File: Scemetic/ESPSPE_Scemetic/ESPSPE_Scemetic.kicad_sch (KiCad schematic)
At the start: 38 parts, among them SW1 RESET, U1 ADIN1110, Y1 25MHz

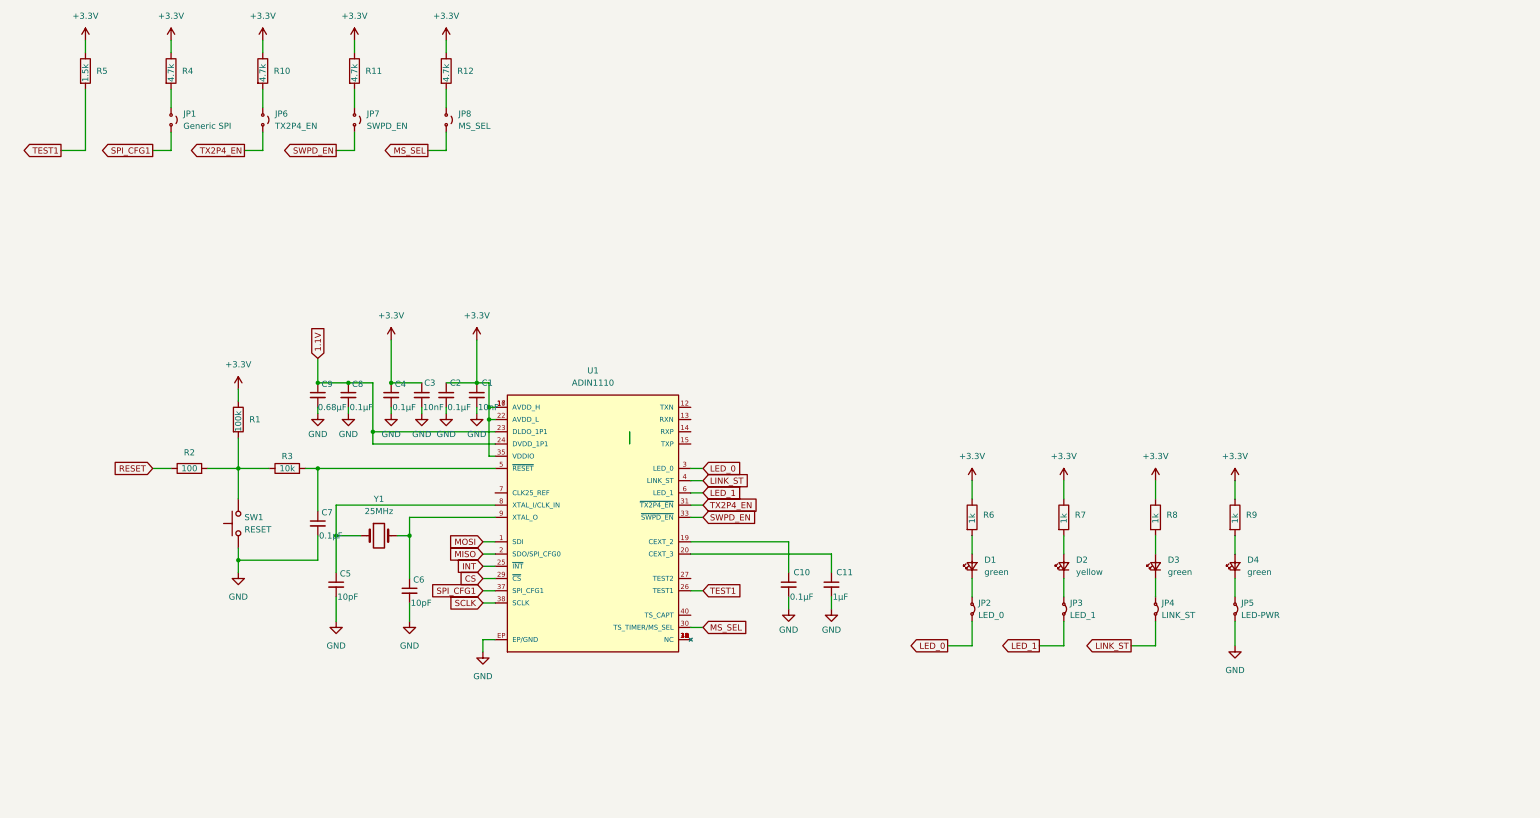
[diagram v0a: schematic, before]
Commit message: added ESP Pinout; Update of Scemetic -> should be ready to search for components
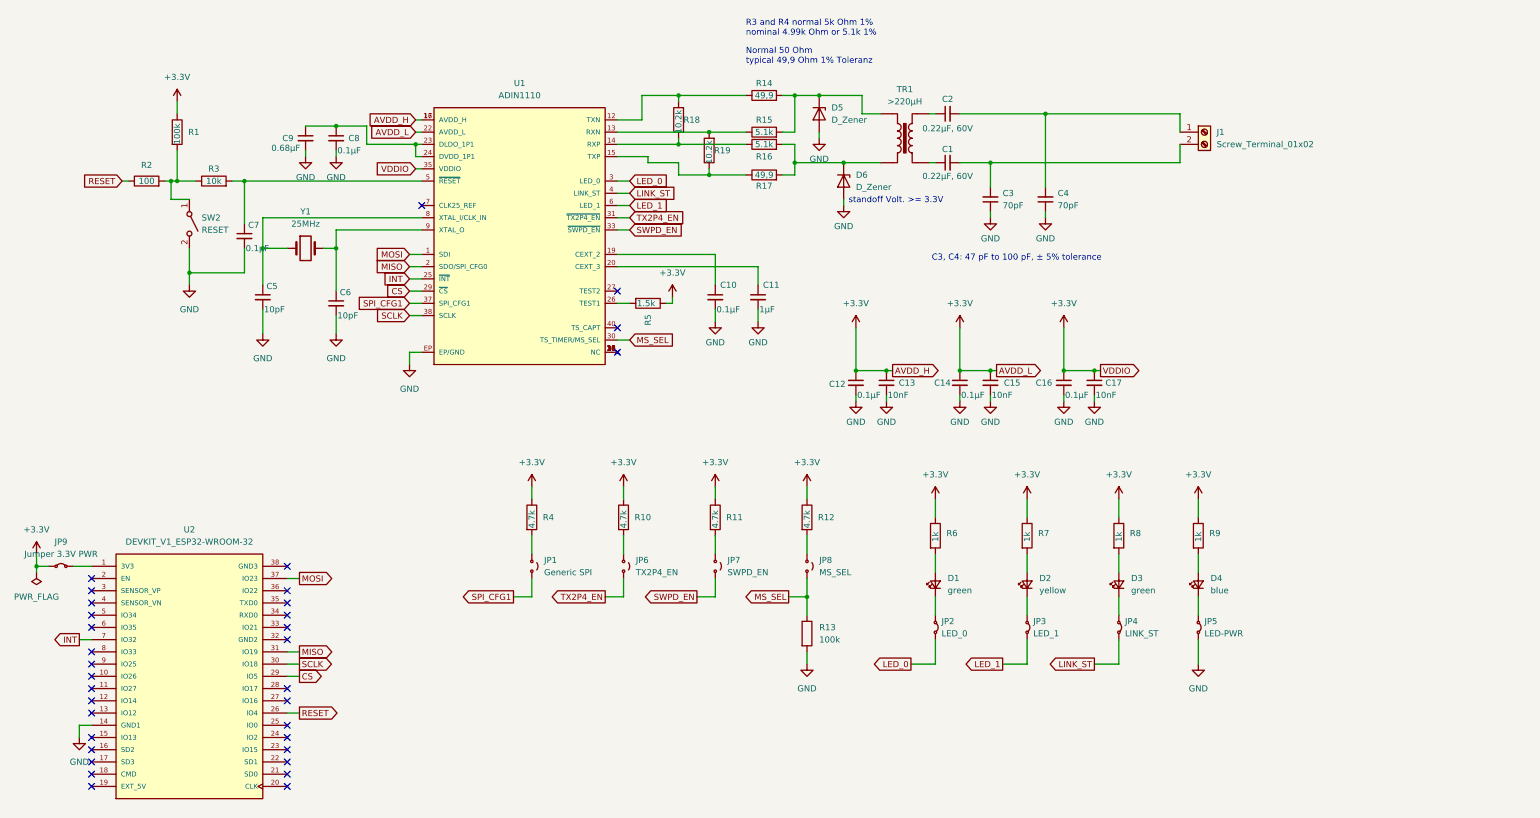
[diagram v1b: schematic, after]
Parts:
- removed SW1: RESET, symbol Switch:SW_Push
- added C12, C14, C16: 0.1µF, symbol Device:C_Small
- added C13, C15, C17: 10nF, symbol Device:C_Small
- added D5, D6: D_Zener, symbol Device:D_Zener
- added J1: Screw_Terminal_01x02, symbol Connector:Screw_Terminal_01x02
- added JP9: Jumper 3.3V PWR, symbol Jumper:Jumper_2_Small_Bridged
- added R13: 100k, symbol Device:R
- added R14, R17: 49,9, symbol Device:R
- added R15, R16: 5.1k, symbol Device:R
- added R18, R19: 10.2k, symbol Device:R
- added SW2: RESET, symbol Switch:SW_SPST
- added TR1: >220µH, symbol Transformer:TRANSF1
- added U2: DEVKIT_V1_ESP32-WROOM-32, DEVKIT_V1_ESP32-WROOM-32:MODULE_DEVKIT_V1_ESP32-WROOM-32, symbol DEVKIT_V1_ESP32-WROOM-32:DEVKIT_V1_ESP32-WROOM-32
- C1: value 10nF -> 0.22µF, 60V
- C2: value 0.1µF -> 0.22µF, 60V
- C3: value 10nF -> 70pF
- C4: value 0.1µF -> 70pF
- D4: value green -> blue
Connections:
- net +3.3V: now also C12.1, C13.1, C14.1, C15.1, C16.1, C17.1, JP9.1 (A); no longer C1.1, C2.1, C3.1, C4.1
- net CS: now also U2.29 (IO5)
- net GND: now also C3.1, C4.1, C12.2, C13.2, C14.2, C15.2, C16.2, C17.2, D5.2 (A), D6.2 (A), R13.2, SW2.2 (B), U2.14 (GND1); no longer C1.2, C2.2, C3.2, C4.2
- net INT: now also U2.7 (IO32)
- net MISO: now also U2.31 (IO19)
- net MOSI: now also U2.37 (IO23)
- net MS_SEL: now also R13.1
- net RESET: now also U2.26 (IO4)
- net SCLK: now also U2.30 (IO18)
- net at R1.2, R2.2, R3.1: now also SW2.1 (A)
- net at U1.12 (TXN): now also R14.1, R18.2
- net at U1.13 (RXN): now also R15.1, R19.2
- net at U1.14 (RXP): now also R16.1, R18.1
- net at U1.15 (TXP): now also R17.1, R19.1
- net 1.1V: no longer names the net of C8.1, C9.1, U1.23 (DLDO_1P1), U1.24 (DVDD_1P1)
- net TEST1: no longer names the net of R5.2, U1.26 (TEST1)
- new net: D5.1 (K), R14.2, R15.2, TR1.1
- new net: C2.2, C4.2, J1.1 (Pin_1)
- new net: JP9.2 (B), U2.1 (3V3)
- new net: C1.1, TR1.3
- new net: C1.2, C3.2, J1.2 (Pin_2)
- new net: C2.1, TR1.4
- new net: D6.1 (K), R16.2, R17.2, TR1.2
- no-connect marks 0 -> 34
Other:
- note added: "C3, C4: 47 pF to 100 pF, ± 5% tolerance"
- note added: "Normal 50 Ohm typical 49,9 Ohm 1% Toleranz"
- note added: "R3 and R4 normal 5k Ohm 1% nominal 4.99k Ohm or 5.1k 1%"
- note added: "standoff Volt. >= 3.3V"
- moved on the sheet: C10, C11, C5, C6, C7, C8, C9, D1, D2, D3, D4, JP1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

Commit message: Schaltplan vollständig
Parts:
- renumbered C7 to C1, C2 to C10, C1 to C11, C14 to C12, C3 to C13, C15 to C14, C4 to C15, C5 to C2, C9 to C3, C8 to C4, C6 to C5, C10 to C6, C11 to C7, C12 to C8, C13 to C9, D5 to D1, D6 to D2, D1 to D3, D2 to D4, D3 to D5, D4 to D6, JP9 to JP1, JP1 to JP2, JP6 to JP3, JP7 to JP4, JP8 to JP5, JP2 to JP6, JP3 to JP7, JP4 to JP8, JP5 to JP9, R2 to R1, R14 to R10, R15 to R11, R16 to R12, R17 to R13, R12 to R14, R13 to R15, R6 to R16, R7 to R17, R8 to R18, R9 to R19, R1 to R2, R10 to R5, R5 to R6, R18 to R7, R19 to R8, R11 to R9, SW2 to SW1, U2 to U1, U1 to U2

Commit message: Schaltplan Footprintzuweisung angefangen
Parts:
- removed TR1: >220µH, symbol Transformer:TRANSF1
- added T1: 749070010, Transformer_SMD_Wurth:T_Wurth_WE-SPE_749070010, symbol Transformer_Wurth_WE-SPE:749070010
- added Y2: CFPX-180_830105863709, Crystal_SMD_Wurth:Y_Wurth_WE-XTAL-CFPX-180, symbol Crystal_Wurth_WE-XTAL:CFPX-180_830105863709
- C1, C10, C11, C12, C13, C14, C15, C16, C17, C2, C3, C4, C5, C6, C7, C8, C9: footprint (none) -> Capacitor_SMD:C_0805_2012Metric_Pad1.18x1.45mm_HandSolder
- D3, D5: footprint (none) -> LED_THT:LED_D3.0mm
- D4: value yellow -> green; footprint (none) -> LED_THT:LED_D3.0mm
- D6: value blue -> green; footprint (none) -> LED_THT:LED_D3.0mm
- J1: footprint (none) -> TerminalBlock_Phoenix:TerminalBlock_Phoenix_MPT-0,5-2-2.54_1x02_P2.54mm_Horizontal
- JP1, JP2, JP3, JP4, JP5, JP6, JP7, JP8, JP9: footprint (none) -> Connector_PinHeader_2.54mm:PinHeader_1x02_P2.54mm_Vertical
- R1, R10, R11, R12, R13, R14, R15, R16, R17, R18, R19, R2, R3, R4, R5, R6, R7, R8, R9: footprint (none) -> Resistor_SMD:R_0805_2012Metric_Pad1.20x1.40mm_HandSolder
- SW1: footprint (none) -> Button_Switch_THT:SW_PUSH_6mm
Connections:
- net at D1.1 (K), R10.2, R11.2: now also T1.1
- net at C11.1: now also T1.3
- net at C10.1: now also T1.2
- net at D2.1 (K), R12.2, R13.2: now also T1.4
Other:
- note added: "Benötigen wir hier eine spezielle Bauform / Marke?"
- note added: "Kondensatoren so nah wie möglich an IC platzieren"
- moved on the sheet: C10, C11, C13, C15, J1

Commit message: Jumper für PWR LED entfernt. Footprint für Traffo und Quartz zugewiesen. Z_Diode 0805 zugewiesen. Platine angefangen zu zeichen -> Bauteile angeordnet
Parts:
- removed JP9: LED-PWR, Connector_PinHeader_2.54mm:PinHeader_1x02_P2.54mm_Vertical, symbol Jumper:Jumper_2_Small_Bridged
- removed Y1: 25MHz, symbol Device:Crystal
- C2, C5: value 10pF -> 15pF
- D1, D2: footprint (none) -> Diode_SMD:D_0805_2012Metric_Pad1.15x1.40mm_HandSolder
- Y2: footprint Crystal_SMD_Wurth:Y_Wurth_WE-XTAL-CFPX-180 -> Crystal_SMD_Wurth:Y_Wurth_WE-XTAL_Quartz-CFPX-180
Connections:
- net GND: now also D6.1 (K), Y2.2 (GND), Y2.4 (GND1)
- net at Y2.1: now also C2.1, U2.8 (XTAL_I/CLK_IN)
- net at Y2.3: now also C5.1, U2.9 (XTAL_O)
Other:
- note added: "25MHz"
- note added: "C13, C15: 47 pF to 100 pF, ± 5% tolerance"
- note removed: "C3, C4: 47 pF to 100 pF, ± 5% tolerance"
- moved on the sheet: C12, C14, C16, C17, C8, C9, D1, D2, Y2

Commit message: Jumper der LEDs entfernt
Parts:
- removed JP6: LED_0, Connector_PinHeader_2.54mm:PinHeader_1x02_P2.54mm_Vertical, symbol Jumper:Jumper_2_Small_Bridged
- removed JP7: LED_1, Connector_PinHeader_2.54mm:PinHeader_1x02_P2.54mm_Vertical, symbol Jumper:Jumper_2_Small_Bridged
- removed JP8: LINK_ST, Connector_PinHeader_2.54mm:PinHeader_1x02_P2.54mm_Vertical, symbol Jumper:Jumper_2_Small_Bridged
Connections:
- net LED_0: now also D3.1 (K)
- net LED_1: now also D4.1 (K)
- net LINK_ST: now also D5.1 (K)
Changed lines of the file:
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@@
 	(wire
 		(pts
-			(xy 210.82 152.4) (xy 210.82 157.48)
+			(xy 210.82 143.51) (xy 210.82 157.48)
 		)
 		(stroke
@@
 	(wire
 		(pts
-			(xy 210.82 143.51) (xy 210.82 147.32)
-		)
-		(stroke
-			(width 0)
-			(type default)
-		)
-	)
-	(wire
-		(pts
 			(xy 33.02 152.4) (xy 35.56 152.4)
 		)
@@
 	(wire
 		(pts
+			(xy 248.92 143.51) (xy 248.92 157.48)
+		)
+		(stroke
+			(width 0)
+			(type default)
+		)
+	)
+	(wire
+		(pts
 			(xy 229.87 134.62) (xy 229.87 138.43)
 		)
@@
 	(wire
 		(pts
-			(xy 229.87 143.51) (xy 229.87 147.32)
-		)
-		(stroke
-			(width 0)
-			(type default)
-		)
-	)
-	(wire
-		(pts
-			(xy 248.92 152.4) (xy 248.92 157.48)
+			(xy 229.87 143.51) (xy 229.87 157.48)
 		)
 		(stroke
@@
 	(wire
 		(pts
-			(xy 229.87 152.4) (xy 229.87 157.48)
-		)
-		(stroke
-			(width 0)
-			(type default)
-		)
-	)
-	(wire
-		(pts
 			(xy 181.61 55.88) (xy 181.61 53.34)
 		)
@@
 	(wire
 		(pts
-			(xy 248.92 143.51) (xy 248.92 147.32)
-		)
-		(stroke
-			(width 0)
-			(type default)
-		)
-	)
-	(wire
-		(pts
 			(xy 151.13 52.07) (xy 144.78 52.07)
 		)
@@
 	)
 	(symbol
-		(lib_id "Jumper:Jumper_2_Small_Bridged")
-		(at 248.92 149.86 270)
-		(unit 1)
-		(exclude_from_sim no)
-		(in_bom yes)
-		(on_board yes)
-		(dnp no)
-		(fields_autoplaced yes)
-		(property "Reference" "JP8"
-			(at 250.19 148.5899 90)
-			(effects
-				(font
-					(size 1.27 1.27)
-				)
-				(justify left)
-			)
-		)
-		(property "Value" "LINK_ST"
-			(at 250.19 151.1299 90)
-			(effects
-				(font
-					(size 1.27 1.27)
-				)
-				(justify left)
-			)
-		)
-		(property "Footprint" "Connector_PinHeader_2.54mm:PinHeader_1x02_P2.54mm_Vertical"
-			(at 248.92 149.86 0)
-			(effects
-				(font
-					(size 1.27 1.27)
-				)
-				(hide yes)
-			)
-		)
-		(property "Datasheet" "~"
-			(at 248.92 149.86 0)
-			(effects
-				(font
-					(size 1.27 1.27)
-				)
-				(hide yes)
-			)
-		)
-		(property "Description" "Jumper, 2-pole, small symbol, bridged"
-			(at 248.92 149.86 0)
-			(effects
-				(font
-					(size 1.27 1.27)
-				)
-				(hide yes)
-			)
-		)
-		(pin "1"
-		)
-		(pin "2"
-		)
-		(instances
-			(project "ESPSPE_Scemetic"
-				(path "/a7aa0af1-99b4-4491-b08a-049990c2f2ac"
-					(reference "JP8")
-					(unit 1)
-				)
-			)
-		)
-	)
-	(symbol
 		(lib_id "Jumper:Jumper_2_Small_Open")
 		(at 127 137.16 270)
@@
 	)
 	(symbol
-		(lib_id "Jumper:Jumper_2_Small_Bridged")
-		(at 229.87 149.86 270)
-		(unit 1)
-		(exclude_from_sim no)
-		(in_bom yes)
-		(on_board yes)
-		(dnp no)
-		(fields_autoplaced yes)
-		(property "Reference" "JP7"
-			(at 231.14 148.5899 90)
-			(effects
-				(font
-					(size 1.27 1.27)
-				)
-				(justify left)
-			)
-		)
-		(property "Value" "LED_1"
-			(at 231.14 151.1299 90)
-			(effects
-				(font
-					(size 1.27 1.27)
-				)
-				(justify left)
-			)
-		)
-		(property "Footprint" "Connector_PinHeader_2.54mm:PinHeader_1x02_P2.54mm_Vertical"
-			(at 229.87 149.86 0)
-			(effects
-				(font
-					(size 1.27 1.27)
-				)
-				(hide yes)
-			)
-		)
-		(property "Datasheet" "~"
-			(at 229.87 149.86 0)
-			(effects
-				(font
-					(size 1.27 1.27)
-				)
-				(hide yes)
-			)
-		)
-		(property "Description" "Jumper, 2-pole, small symbol, bridged"
-			(at 229.87 149.86 0)
-			(effects
-				(font
-					(size 1.27 1.27)
-				)
-				(hide yes)
-			)
-		)
-		(pin "1"
-		)
-		(pin "2"
-		)
-		(instances
-			(project "ESPSPE_Scemetic"
-				(path "/a7aa0af1-99b4-4491-b08a-049990c2f2ac"
-					(reference "JP7")
-					(unit 1)
-				)
-			)
-		)
-	)
-	(symbol
 		(lib_id "power:GND")
 		(at 222.25 104.14 0)
@@
 					(unit 1)
 				)
-			)
-		)
-	)
-	(symbol
-		(lib_id "Jumper:Jumper_2_Small_Bridged")
-		(at 210.82 149.86 270)
-		(unit 1)
-		(exclude_from_sim no)
-		(in_bom yes)
-		(on_board yes)
-		(dnp no)
-		(fields_autoplaced yes)
-		(property "Reference" "JP6"
-			(at 212.09 148.5899 90)
-			(effects
-				(font
-					(size 1.27 1.27)
-				)
-				(justify left)
-			)
-		)
-		(property "Value" "LED_0"
-			(at 212.09 151.1299 90)
-			(effects
-				(font
-					(size 1.27 1.27)
-				)
-				(justify left)
-			)
-		)
-		(property "Footprint" "Connector_PinHeader_2.54mm:PinHeader_1x02_P2.54mm_Vertical"
-			(at 210.82 149.86 0)
-			(effects
-				(font
-					(size 1.27 1.27)
-				)
-				(hide yes)
-			)
-		)
-		(property "Datasheet" "~"
-			(at 210.82 149.86 0)
-			(effects
-				(font
-					(size 1.27 1.27)
-				)
-				(hide yes)
-			)
-		)
-		(property "Description" "Jumper, 2-pole, small symbol, bridged"
-			(at 210.82 149.86 0)
-			(effects
-				(font
-					(size 1.27 1.27)
-				)
-				(hide yes)
-			)
-		)
-		(pin "1"
-		)
-		(pin "2"
-		)
-		(instances
-			(project ""
-				(path "/a7aa0af1-99b4-4491-b08a-049990c2f2ac"
-					(reference "JP6")
-					(unit 1)
-				)

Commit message: Z Dioden hinzugefügt
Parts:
- removed D1, D2: D_Zener, Diode_SMD:D_0805_2012Metric_Pad1.15x1.40mm_HandSolder, symbol Device:D_Zener
- added D1, D2, D7, D8: UDZUVFHTE-175.6B, KiCad_ZDiode_8pf:UDZUVFHTE1756B, symbol UDZUVFHTE-175_6B:UDZUVFHTE-175.6B
- added J2: Conn_01x01_Pin, Connector_PinHeader_2.54mm:PinHeader_1x01_P2.54mm_Vertical, symbol Connector:Conn_01x01_Pin
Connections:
- net GND: now also D1.2 (A), D7.2 (A)
- net at R10.2, R11.2, T1.1: now also D7.1 (K)
- net at C10.2, C15.2, J1.1 (Pin_1): now also D8.2 (A)
- net at C11.2, C13.2, J1.2 (Pin_2): now also D2.2 (A)
- net at R12.2, R13.2, T1.4: now also D1.1 (K)
- net at U1.19 (EXT_5V): now also J2.1 (Pin_1)
- new net: D2.1 (K), D8.1 (K)
- no-connect marks 34 -> 33
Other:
- moved on the sheet: C15, J1

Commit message: Schönifizierung des Netzwerkes; Dioden THT zu SMD gewechselt
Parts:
- D3, D4, D5, D6: footprint LED_THT:LED_D3.0mm -> LED_SMD:LED_0805_2012Metric_Pad1.15x1.40mm_HandSolder
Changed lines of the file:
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@@
 			)
 		)
-		(property "Footprint" "LED_THT:LED_D3.0mm"
+		(property "Footprint" "LED_SMD:LED_0805_2012Metric_Pad1.15x1.40mm_HandSolder"
 			(at 265.43 140.97 90)
 			(effects
@@
 			)
 		)
-		(property "Footprint" "LED_THT:LED_D3.0mm"
+		(property "Footprint" "LED_SMD:LED_0805_2012Metric_Pad1.15x1.40mm_HandSolder"
 			(at 229.87 140.97 90)
 			(effects
@@
 			)
 		)
-		(property "Footprint" "LED_THT:LED_D3.0mm"
+		(property "Footprint" "LED_SMD:LED_0805_2012Metric_Pad1.15x1.40mm_HandSolder"
 			(at 248.92 140.97 90)
 			(effects
@@
 			)
 		)
-		(property "Footprint" "LED_THT:LED_D3.0mm"
+		(property "Footprint" "LED_SMD:LED_0805_2012Metric_Pad1.15x1.40mm_HandSolder"
 			(at 210.82 140.97 90)
 			(effects
